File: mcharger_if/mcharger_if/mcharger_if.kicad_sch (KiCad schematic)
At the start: 43 parts, among them J1 Conn_01x02_Pin, J2 Conn_01x02_Pin, J3 Conn_01x04_Pin, J4 Conn_01x05_Pin, Q1 IRF5210, Q2 IRF5210, Q3 BSS123, Q4 SI2300DS

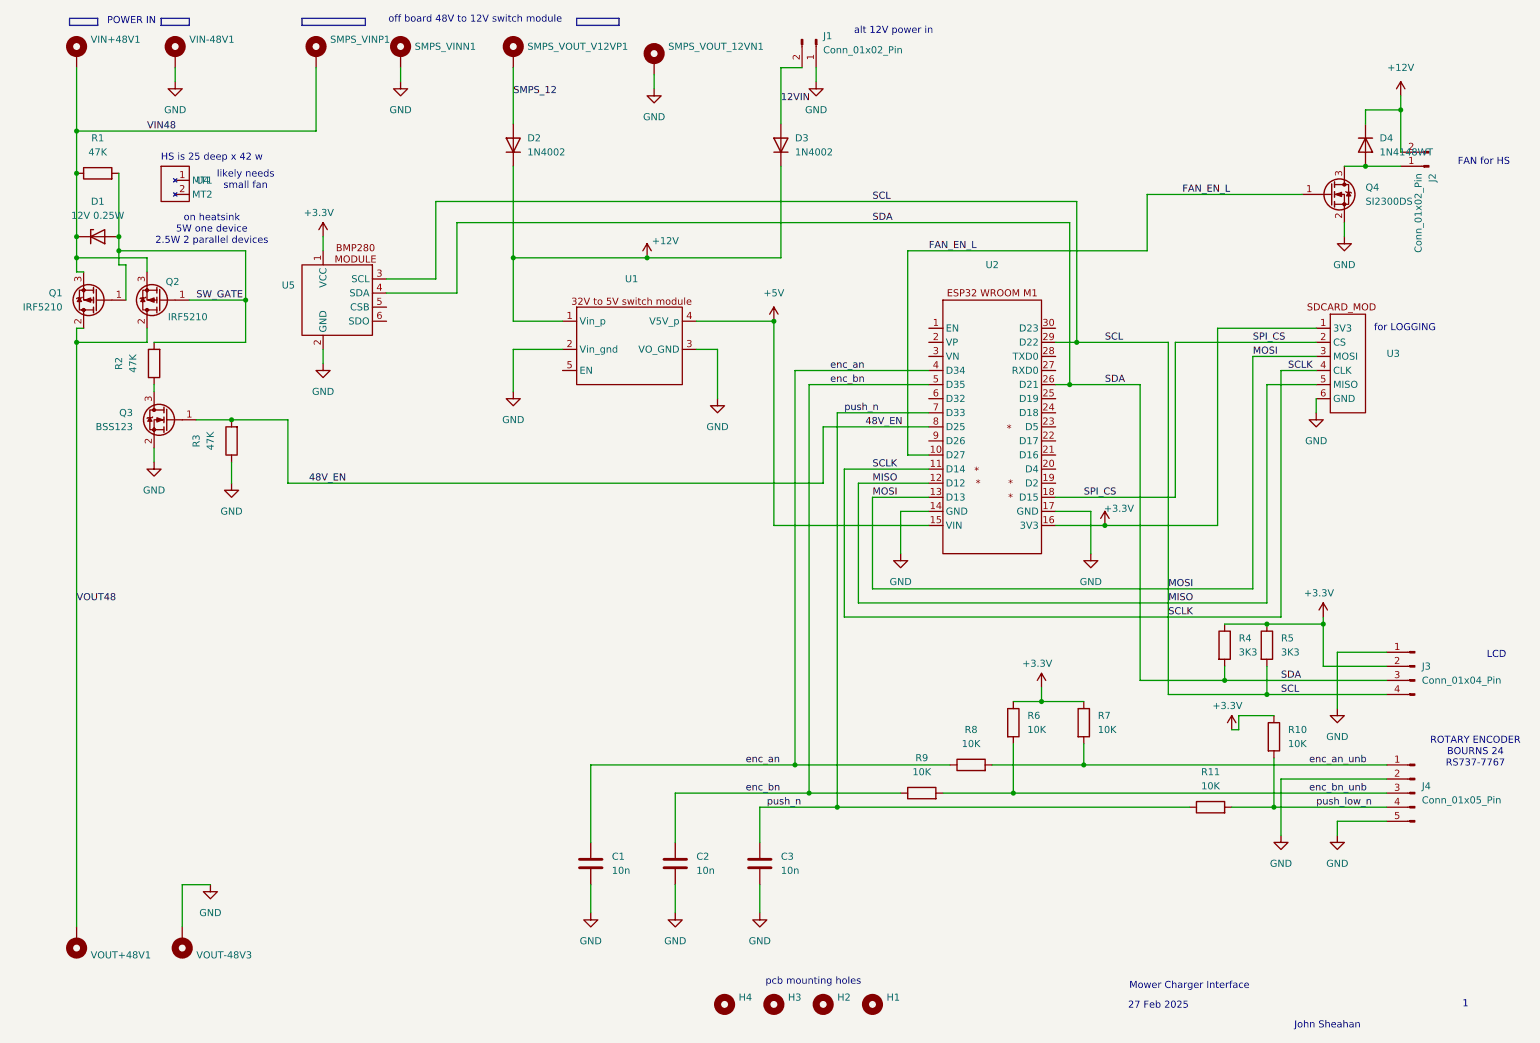
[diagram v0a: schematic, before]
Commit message: add a top level schematic
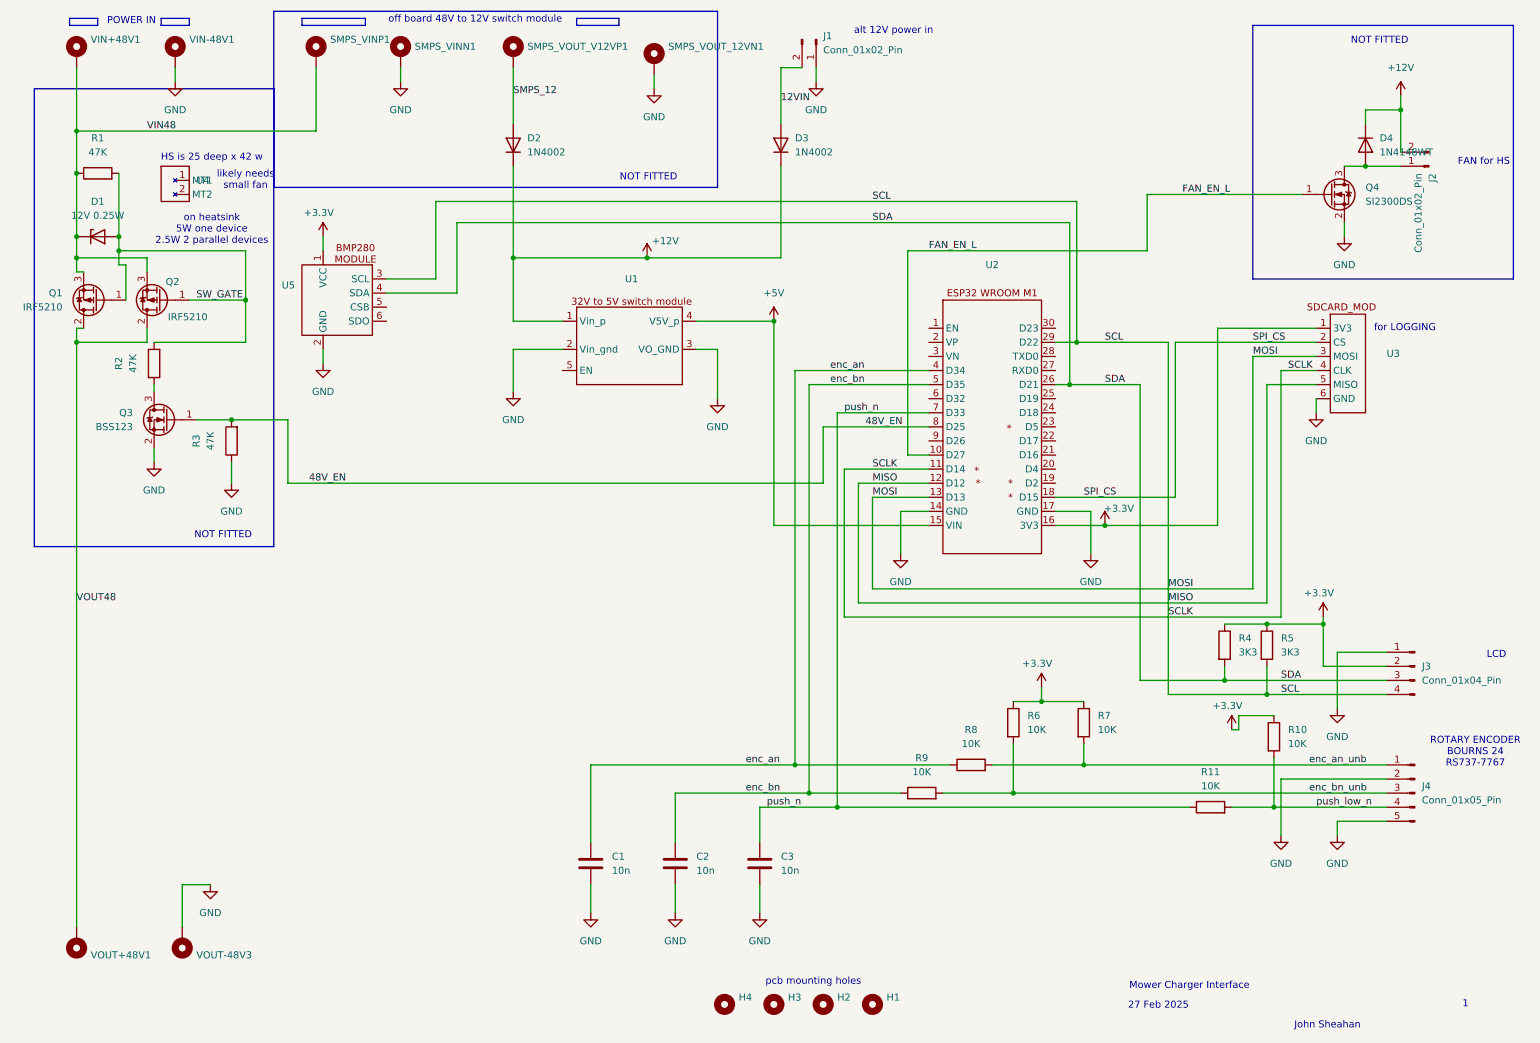
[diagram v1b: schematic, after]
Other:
- note added: "NOT FITTED"
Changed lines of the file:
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@@
 (kicad_sch
-	(version 20231120)
+	(version 20250114)
 	(generator "eeschema")
-	(generator_version "8.0")
+	(generator_version "9.0")
 	(paper "A4")
+	(rectangle
+		(start 113.03 15.24)
+		(end 120.65 16.51)
+		(stroke
+			(width 0)
+			(type default)
+		)
+		(fill
+			(type none)
+		)
+	)
+	(rectangle
+		(start 15.24 27.94)
+		(end 58.42 110.49)
+		(stroke
+			(width 0)
+			(type default)
+		)
+		(fill
+			(type none)
+		)
+	)
+	(rectangle
+		(start 234.95 16.51)
+		(end 281.94 62.23)
+		(stroke
+			(width 0)
+			(type default)
+		)
+		(fill
+			(type none)
+		)
+	)
+	(rectangle
+		(start 21.59 15.24)
+		(end 26.67 16.51)
+		(stroke
+			(width 0)
+			(type default)
+		)
+		(fill
+			(type none)
+		)
+	)
+	(rectangle
+		(start 63.5 15.24)
+		(end 74.93 16.51)
+		(stroke
+			(width 0)
+			(type default)
+		)
+		(fill
+			(type none)
+		)
+	)
+	(rectangle
+		(start 58.42 13.97)
+		(end 138.43 45.72)
+		(stroke
+			(width 0)
+			(type default)
+		)
+		(fill
+			(type none)
+		)
+	)
+	(rectangle
+		(start 38.1 15.24)
+		(end 43.18 16.51)
+		(stroke
+			(width 0)
+			(type default)
+		)
+		(fill
+			(type none)
+		)
+	)
+	(text "likely needs\nsmall fan "
+		(exclude_from_sim no)
+		(at 53.34 44.45 0)
+		(effects
+			(font
+				(size 1.27 1.27)
+			)
+		)
+	)
+	(text "for LOGGING"
+		(exclude_from_sim no)
+		(at 262.382 71.12 0)
+		(effects
+			(font
+				(size 1.27 1.27)
+			)
+		)
+	)
+	(text "NOT FITTED"
+		(exclude_from_sim no)
+		(at 125.984 43.942 0)
+		(effects
+			(font
+				(size 1.27 1.27)
+			)
+		)
+	)
+	(text "POWER IN"
+		(exclude_from_sim no)
+		(at 32.766 15.748 0)
+		(effects
+			(font
+				(size 1.27 1.27)
+			)
+		)
+	)
+	(text "NOT FITTED"
+		(exclude_from_sim no)
+		(at 49.276 108.458 0)
+		(effects
+			(font
+				(size 1.27 1.27)
+			)
+		)
+	)
+	(text "1"
+		(exclude_from_sim no)
+		(at 273.304 193.04 0)
+		(effects
+			(font
+				(size 1.27 1.27)
+			)
+		)
+	)
+	(text "FAN for HS"
+		(exclude_from_sim no)
+		(at 276.606 41.148 0)
+		(effects
+			(font
+				(size 1.27 1.27)
+			)
+		)
+	)
+	(text "27 Feb 2025"
+		(exclude_from_sim no)
+		(at 217.932 193.294 0)
+		(effects
+			(font
+				(size 1.27 1.27)
+			)
+		)
+	)
+	(text "John Sheahan"
+		(exclude_from_sim no)
+		(at 248.412 196.85 0)
+		(effects
+			(font
+				(size 1.27 1.27)
+			)
+		)
+	)
+	(text "Mower Charger Interface"
+		(exclude_from_sim no)
+		(at 223.52 189.738 0)
+		(effects
+			(font
+				(size 1.27 1.27)
+			)
+		)
+	)
+	(text "NOT FITTED"
+		(exclude_from_sim no)
+		(at 257.81 19.304 0)
+		(effects
+			(font
+				(size 1.27 1.27)
+			)
+		)
+	)
+	(text "HS is 25 deep x 42 w"
+		(exclude_from_sim no)
+		(at 47.244 40.386 0)
+		(effects
+			(font
+				(size 1.27 1.27)
+			)
+		)
+	)
+	(text "pcb mounting holes"
+		(exclude_from_sim no)
+		(at 155.702 188.976 0)
+		(effects
+			(font
+				(size 1.27 1.27)
+			)
+		)
+	)
+	(text "off board 48V to 12V switch module"
+		(exclude_from_sim no)
+		(at 94.742 15.494 0)
+		(effects
+			(font
+				(size 1.27 1.27)
+			)
+		)
+	)
+	(text "LCD"
+		(exclude_from_sim no)
+		(at 278.892 130.048 0)
+		(effects
+			(font
+				(size 1.27 1.27)
+			)
+		)
+	)
+	(text "on heatsink \n5W one device\n2.5W 2 parallel devices"
+		(exclude_from_sim no)
+		(at 47.244 53.34 0)
+		(effects
+			(font
+				(size 1.27 1.27)
+			)
+		)
+	)
+	(text "ROTARY ENCODER \nBOURNS 24\nRS737-7767"
+		(exclude_from_sim no)
+		(at 275.082 147.574 0)
+		(effects
+			(font
+				(size 1.27 1.27)
+			)
+		)
+	)
+	(text "alt 12V power in"
+		(exclude_from_sim no)
+		(at 170.18 17.526 0)
+		(effects
+			(font
+				(size 1.27 1.27)
+			)
+		)
+	)
 	(junction
 		(at 229.87 134.62)
@@
 		)
 	)
-	(rectangle
-		(start 113.03 15.24)
-		(end 120.65 16.51)
-		(stroke
-			(width 0)
-			(type default)
-		)
-		(fill
-			(type none)
-		)
-	)
-	(rectangle
-		(start 21.59 15.24)
-		(end 26.67 16.51)
-		(stroke
-			(width 0)
-			(type default)
-		)
-		(fill
-			(type none)
-		)
-	)
-	(rectangle
-		(start 63.5 15.24)
-		(end 74.93 16.51)
-		(stroke
-			(width 0)
-			(type default)
-		)
-		(fill
-			(type none)
-		)
-	)
-	(rectangle
-		(start 38.1 15.24)
-		(end 43.18 16.51)
-		(stroke
-			(width 0)
-			(type default)
-		)
-		(fill
-			(type none)
-		)
-	)
-	(text "likely needs\nsmall fan "
-		(exclude_from_sim no)
-		(at 53.34 44.45 0)
-		(effects
-			(font
-				(size 1.27 1.27)
-			)
-		)
-	)
-	(text "for LOGGING"
-		(exclude_from_sim no)
-		(at 262.382 71.12 0)
-		(effects
-			(font
-				(size 1.27 1.27)
-			)
-		)
-	)
-	(text "POWER IN"
-		(exclude_from_sim no)
-		(at 32.766 15.748 0)
-		(effects
-			(font
-				(size 1.27 1.27)
-			)
-		)
-	)
-	(text "1"
-		(exclude_from_sim no)
-		(at 273.304 193.04 0)
-		(effects
-			(font
-				(size 1.27 1.27)
-			)
-		)
-	)
-	(text "FAN for HS"
-		(exclude_from_sim no)
-		(at 276.606 41.148 0)
-		(effects
-			(font
-				(size 1.27 1.27)
-			)
-		)
-	)
-	(text "27 Feb 2025"
-		(exclude_from_sim no)
-		(at 217.932 193.294 0)
-		(effects
-			(font
-				(size 1.27 1.27)
-			)
-		)
-	)
-	(text "John Sheahan"
-		(exclude_from_sim no)
-		(at 248.412 196.85 0)
-		(effects
-			(font
-				(size 1.27 1.27)
-			)
-		)
-	)
-	(text "Mower Charger Interface"
-		(exclude_from_sim no)
-		(at 223.52 189.738 0)
-		(effects
-			(font
-				(size 1.27 1.27)
-			)
-		)
-	)
-	(text "HS is 25 deep x 42 w"
-		(exclude_from_sim no)
-		(at 47.244 40.386 0)
-		(effects
-			(font
-				(size 1.27 1.27)
-			)
-		)
-	)
-	(text "pcb mounting holes"
-		(exclude_from_sim no)
-		(at 155.702 188.976 0)
-		(effects
-			(font
-				(size 1.27 1.27)
-			)
-		)
-	)
-	(text "off board 48V to 12V switch module"
-		(exclude_from_sim no)
-		(at 94.742 15.494 0)
-		(effects
-			(font
-				(size 1.27 1.27)
-			)
-		)
-	)
-	(text "LCD"
-		(exclude_from_sim no)
-		(at 278.892 130.048 0)
-		(effects
-			(font
-				(size 1.27 1.27)
-			)
-		)
-	)
-	(text "on heatsink \n5W one device\n2.5W 2 parallel devices"
-		(exclude_from_sim no)
-		(at 47.244 53.34 0)
-		(effects
-			(font
-				(size 1.27 1.27)
-			)
-		)
-	)
-	(text "ROTARY ENCODER \nBOURNS 24\nRS737-7767"
-		(exclude_from_sim no)
-		(at 275.082 147.574 0)
-		(effects
-			(font
-				(size 1.27 1.27)
-			)
-		)
-	)
-	(text "alt 12V power in"
-		(exclude_from_sim no)
-		(at 170.18 17.526 0)
-		(effects
-			(font
-				(size 1.27 1.27)
-			)
-		)
-	)
 	(label "SPI_CS"
 		(at 234.95 73.66 0)
@@
 		)
 	)
+	(embedded_fonts no)
 )
